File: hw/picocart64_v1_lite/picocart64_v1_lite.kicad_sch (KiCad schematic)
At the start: 10 parts, among them J1 Conn_01x04, J2 Conn_01x07, J3 Conn_01x02, J4 Conn_01x01, J5 Conn_01x01, Q1 BSS84, U1 Pico, U4 N64-Cartridge

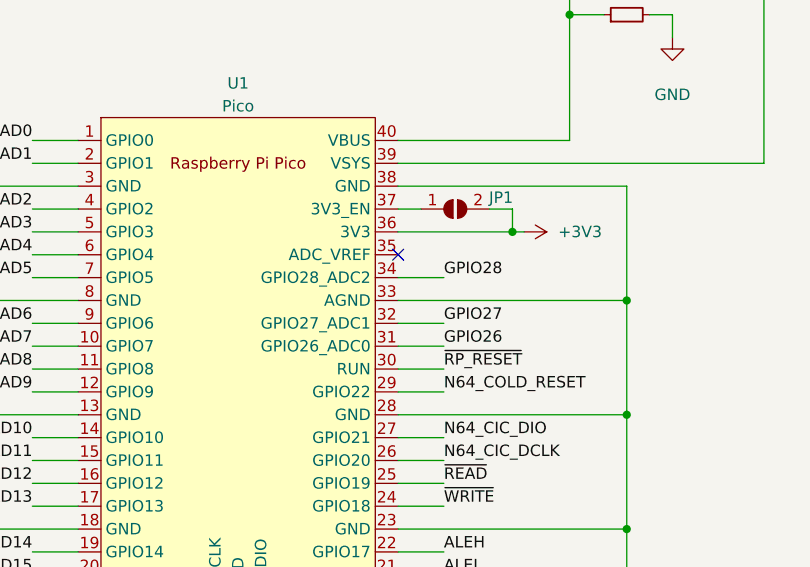
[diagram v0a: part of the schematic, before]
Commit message: Changes to v1 lite board to allow drop in weact as default instead of pico.
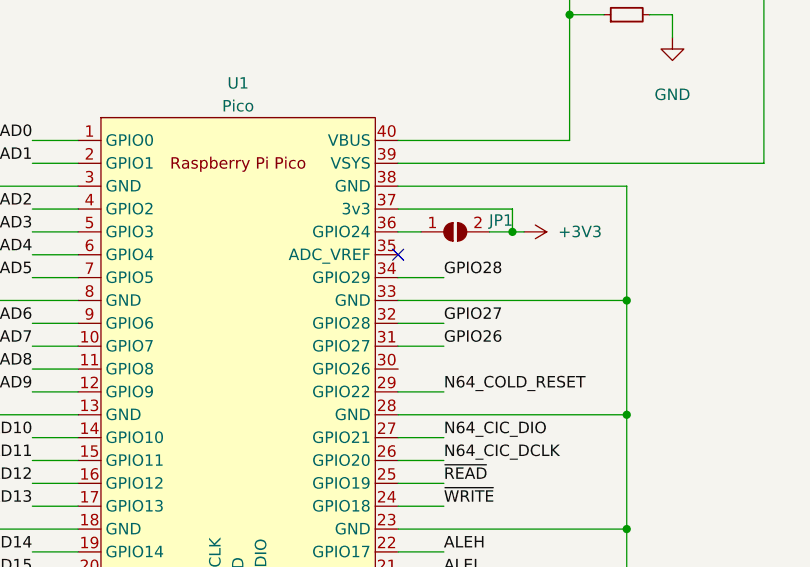
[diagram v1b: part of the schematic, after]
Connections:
- net +3V3: now also U1.37 (3v3); no longer U1.36 (3V3)
- net at JP1.1 (A): now also U1.36 (GPIO24); no longer U1.37 (3V3_EN)
- net ~{RP_RESET}: no longer names the net of U1.30 (GPIO26)
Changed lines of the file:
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@@
+    (stroke (width 0) (type default) (color 0 0 0 0))
+  )
+  (wire (pts (xy 76.2 58.42) (xy 78.74 58.42))
     (stroke (width 0) (type default) (color 0 0 0 0))
   )
@@
     (stroke (width 0) (type default) (color 0 0 0 0))
   )
-  (wire (pts (xy 71.12 73.66) (xy 66.04 73.66))
-    (stroke (width 0) (type default) (color 0 0 0 0))
-  )
   (wire (pts (xy 106.68 50.8) (xy 66.04 50.8))
     (stroke (width 0) (type default) (color 0 0 0 0))
@@
     (stroke (width 0) (type default) (color 0 0 0 0))
   )
-  (wire (pts (xy 76.2 55.88) (xy 78.74 55.88))
-    (stroke (width 0) (type default) (color 0 0 0 0))
-  )
   (wire (pts (xy 16.51 66.04) (xy 30.48 66.04))
     (stroke (width 0) (type default) (color 0 0 0 0))
@@
     (stroke (width 0) (type default) (color 0 0 0 0))
   )
-  (wire (pts (xy 66.04 58.42) (xy 78.74 58.42))
+  (wire (pts (xy 66.04 58.42) (xy 68.58 58.42))
     (stroke (width 0) (type default) (color 0 0 0 0))
   )
@@
     (stroke (width 0) (type default) (color 0 0 0 0))
   )
-  (wire (pts (xy 66.04 55.88) (xy 68.58 55.88))
+  (wire (pts (xy 66.04 55.88) (xy 78.74 55.88))
     (stroke (width 0) (type default) (color 0 0 0 0))
   )
@@
   )
   (label "N64_INT" (at 267.97 71.12 0)
-    (effects (font (size 1.27 1.27)) (justify left bottom))
-  )
-  (label "~{RP_RESET}" (at 71.12 73.66 0)
     (effects (font (size 1.27 1.27)) (justify left bottom))
   )
@@
     (pin "1")
   )
-  (symbol (lib_id "Jumper:SolderJumper_2_Open") (at 72.39 55.88 0) (unit 1)
-    (in_bom yes) (on_board yes)
-    (property "Reference" "JP1" (id 0) (at 77.47 54.61 0))
-    (property "Value" "SolderJumper_2_Open" (id 1) (at 103.505 55.245 0)
-      (effects (font (size 1.27 1.27)) hide)
-    )
-    (property "Footprint" "Jumper:SolderJumper-2_P1.3mm_Open_RoundedPad1.0x1.5mm" (id 2) (at 72.39 55.88 0)
-      (effects (font (size 1.27 1.27)) hide)
-    )
-    (property "Datasheet" "~" (id 3) (at 72.39 55.88 0)
-      (effects (font (size 1.27 1.27)) hide)
-    )
-    (pin "1")
-    (pin "2")
-  )
   (symbol (lib_id "power:+3V3") (at 115.57 148.59 0) (unit 1)
     (in_bom yes) (on_board yes) (fields_autoplaced)
@@
     )
     (pin "1")
+  )
+  (symbol (lib_id "Jumper:SolderJumper_2_Open") (at 72.39 58.42 0) (unit 1)
+    (in_bom yes) (on_board yes)
+    (property "Reference" "JP1" (id 0) (at 77.47 57.15 0))
+    (property "Value" "SolderJumper_2_Open" (id 1) (at 103.505 57.785 0)
+      (effects (font (size 1.27 1.27)) hide)
+    )
+    (property "Footprint" "Jumper:SolderJumper-2_P1.3mm_Open_RoundedPad1.0x1.5mm" (id 2) (at 72.39 58.42 0)
+      (effects (font (size 1.27 1.27)) hide)
+    )
+    (property "Datasheet" "~" (id 3) (at 72.39 58.42 0)
+      (effects (font (size 1.27 1.27)) hide)
+    )
+    (pin "1")
+    (pin "2")
   )
   (symbol (lib_id "Transistor_FET:BSS84") (at 85.09 26.67 90) (unit 1)
@@
       (reference "J5") (unit 1) (value "Conn_01x01") (footprint "Connector_PinHeader_2.54mm:PinHeader_1x01_P2.54mm_Vertical")
     )
-    (path "/26be3cc2-c297-45a0-b245-5214add93bfb"
+    (path "/473bf731-aa75-47f2-a623-1e19252b1461"
       (reference "JP1") (unit 1) (value "SolderJumper_2_Open") (footprint "Jumper:SolderJumper-2_P1.3mm_Open_RoundedPad1.0x1.5mm")
     )
